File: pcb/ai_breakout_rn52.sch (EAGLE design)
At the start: 8 parts, among them IC1 RN-52, J1 1X20, J2 1X20

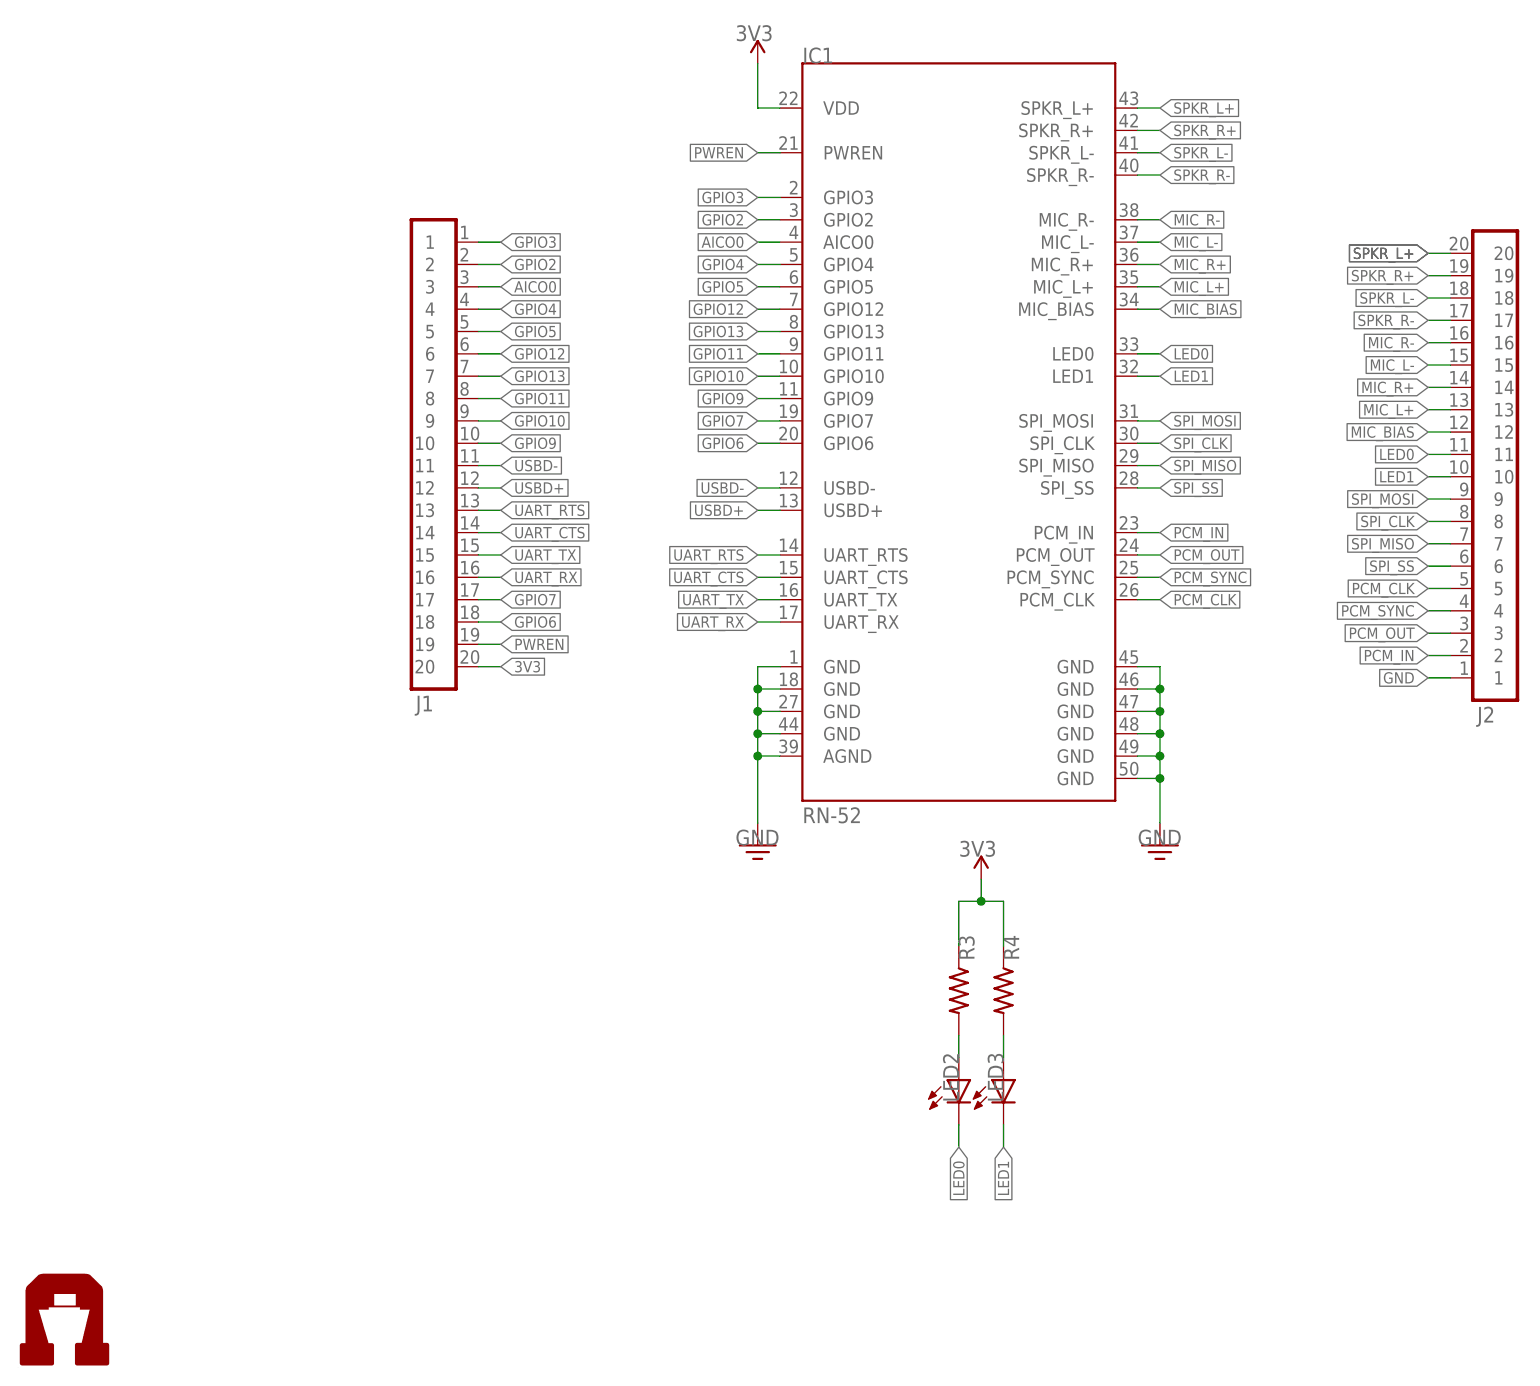
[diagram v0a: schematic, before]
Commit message: added BOM
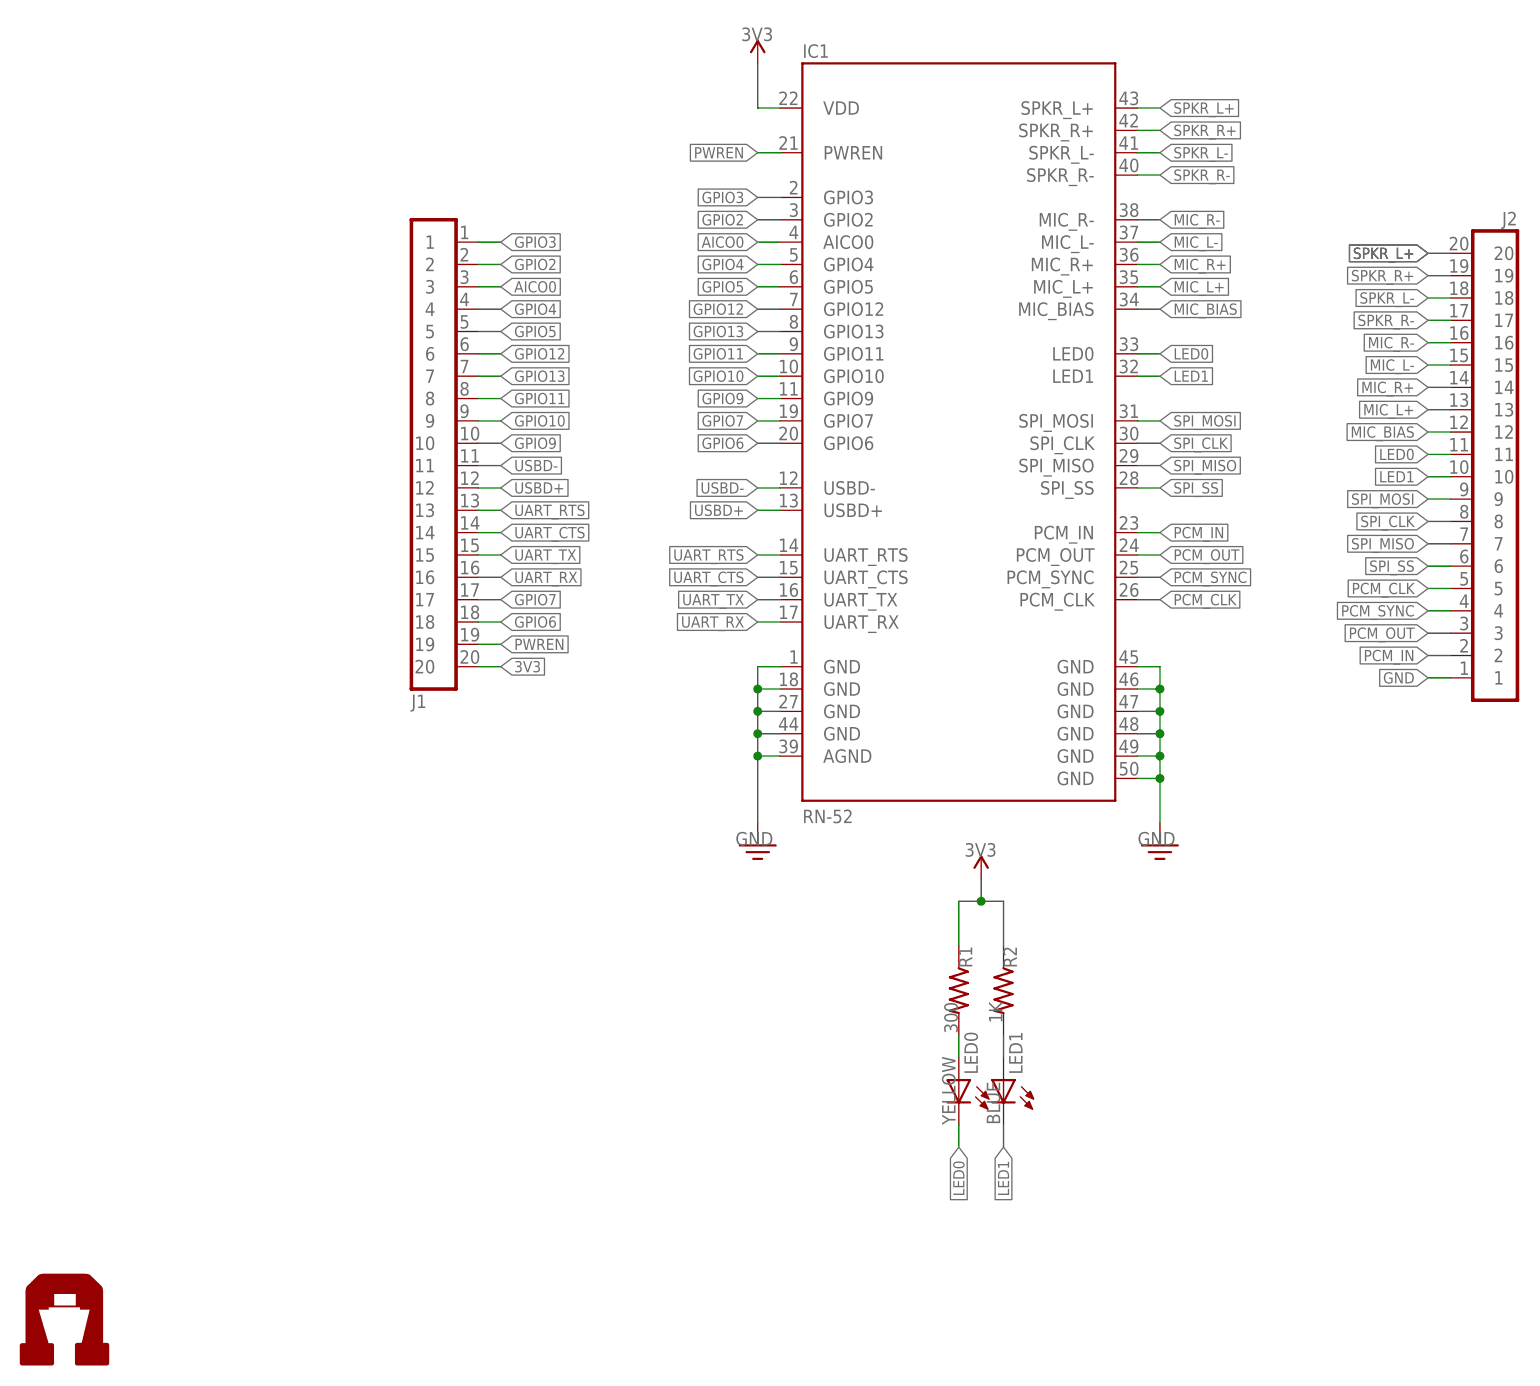
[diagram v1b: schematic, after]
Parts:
- removed R3, R4: (no value), Ai_Passives:RES
- added R1: 300, Ai_Passives:RES0603
- added R2: 1K, Ai_Passives:RES0603
- LED0: value (none) -> YELLOW
- LED1: value (none) -> BLUE
- renumbered LED2 to LED0, LED3 to LED1
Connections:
- net 3V3: now also R1.1, R2.1; no longer R3.1, R4.1
- net N$6: now also R1.2; no longer R3.2
- net N$7: now also R2.2; no longer R4.2
